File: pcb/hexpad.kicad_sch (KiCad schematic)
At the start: 12 parts, among them SW1 SW_Push, SW2 SW_Push, SW3 SW_Push, SW4 SW_Push, SW5 SW_Push, SW6 SW_Push, U1 XIAO-RP2040

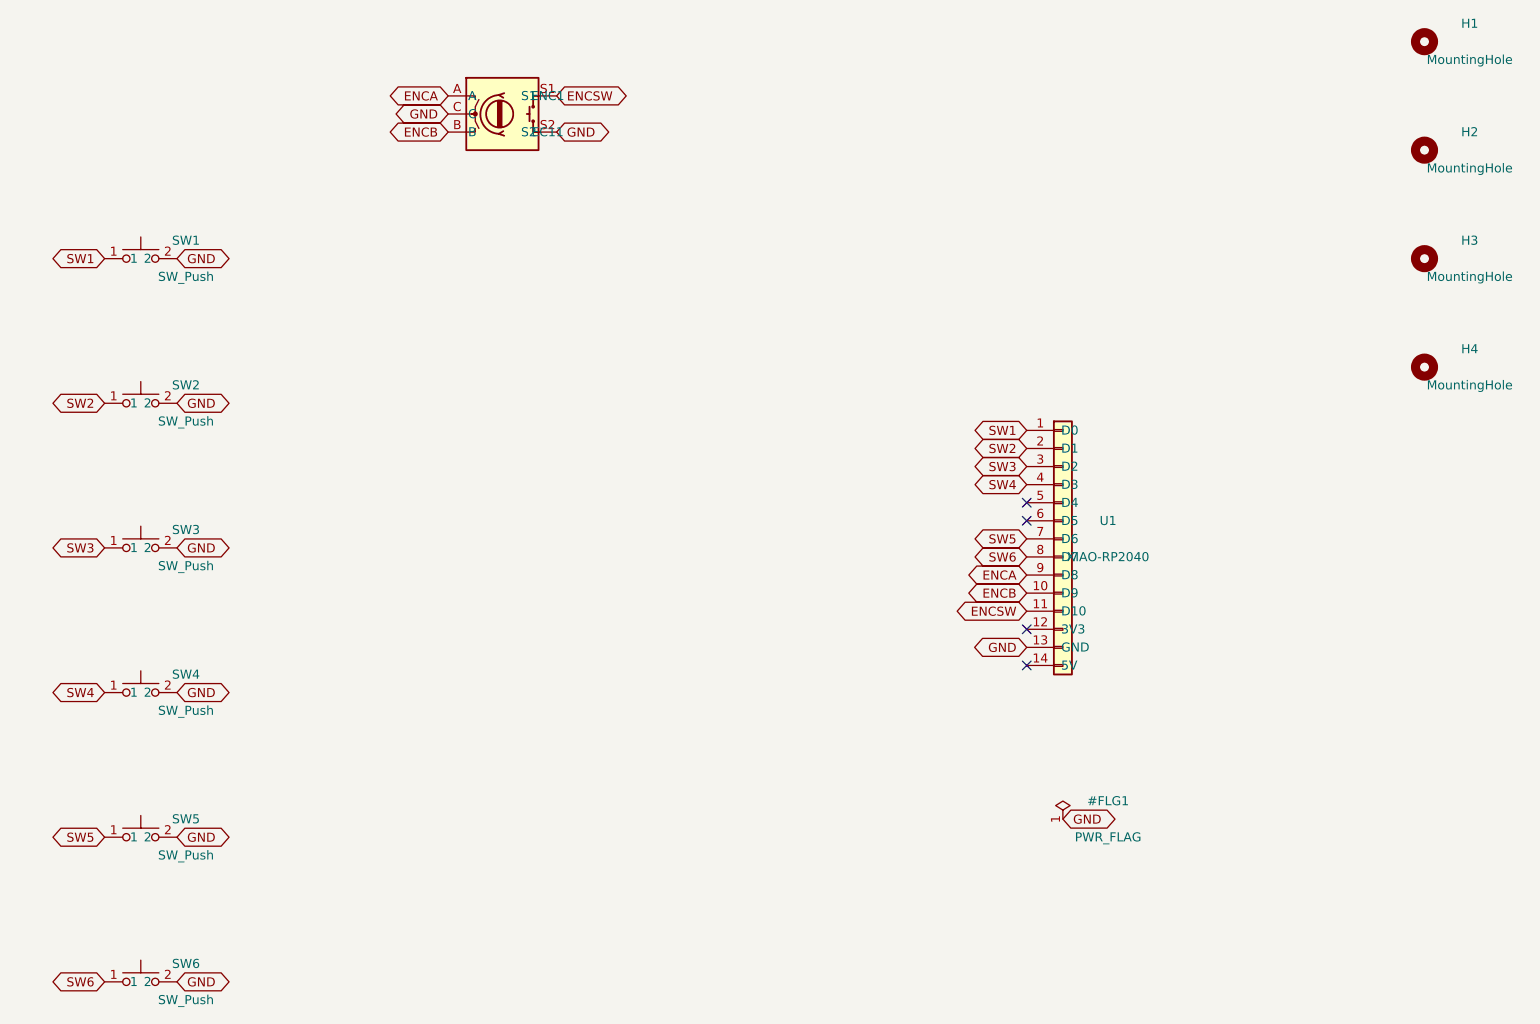
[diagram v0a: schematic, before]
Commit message: schematic: add wire stubs so labels don't overlap symbols
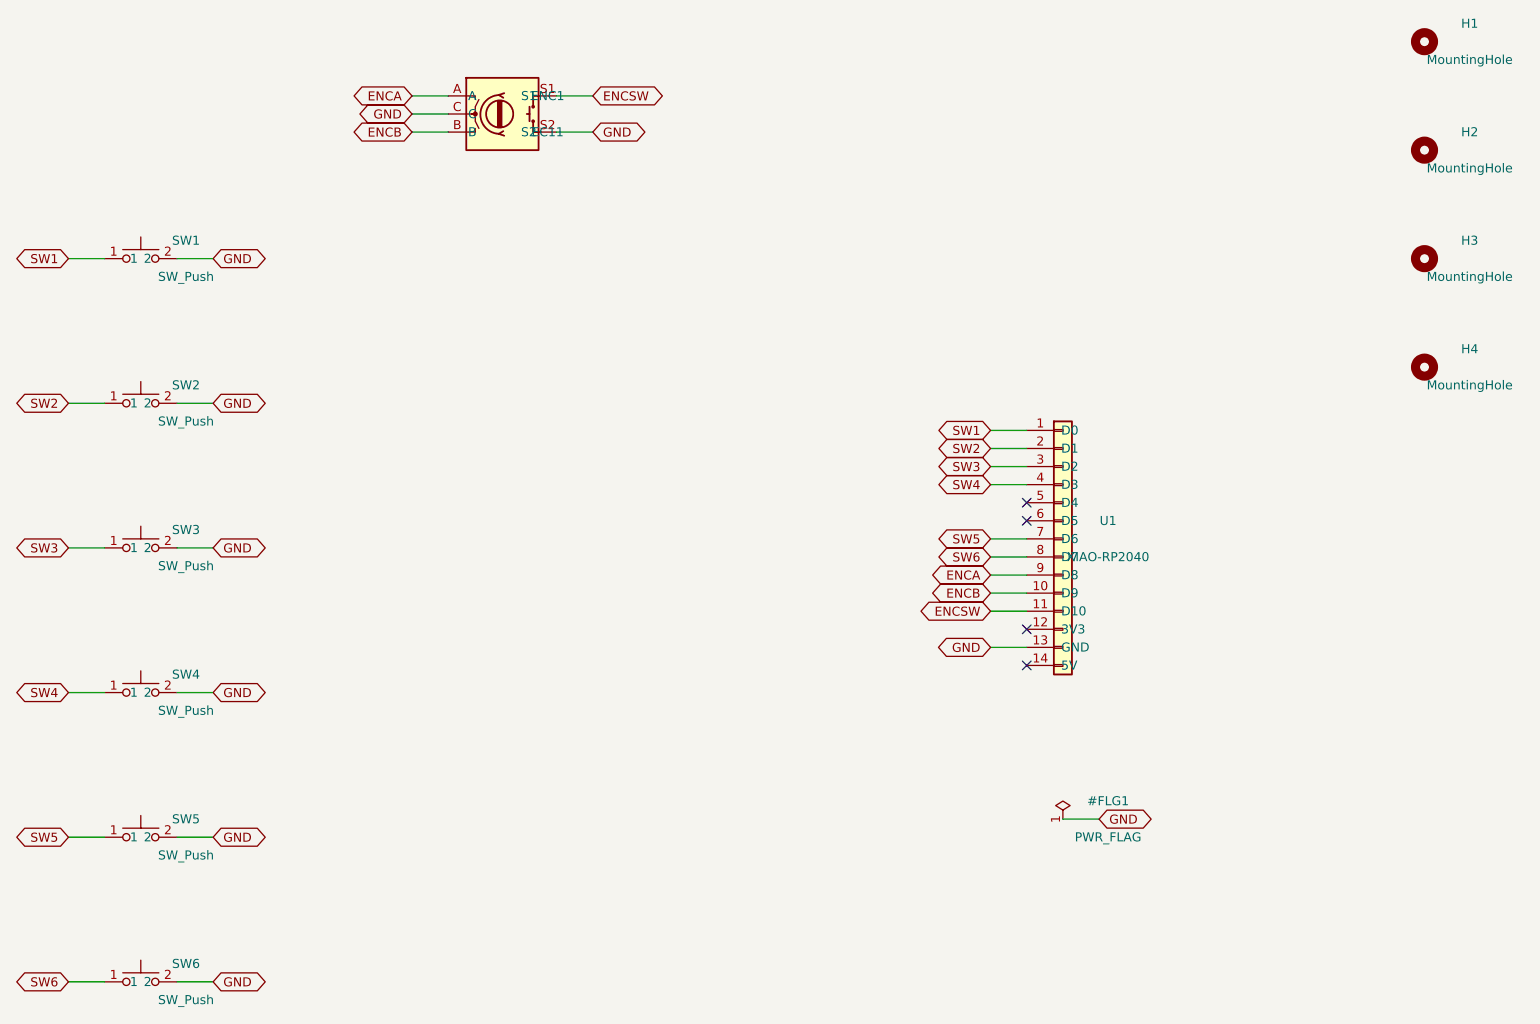
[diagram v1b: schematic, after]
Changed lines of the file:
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@@
   (no_connect (at 185.42 123.19))
   (no_connect (at 185.42 128.26999999999998))
-  (global_label "SW1" (shape bidirectional) (at 185.42 95.25 180)
+  (wire (pts (xy 185.42000000000002 95.25) (xy 180.34 95.25))
+    (stroke (width 0.0))
+  )
+  (wire (pts (xy 185.42000000000002 97.79) (xy 180.34 97.79))
+    (stroke (width 0.0))
+  )
+  (wire (pts (xy 185.42000000000002 100.33) (xy 180.34 100.33))
+    (stroke (width 0.0))
+  )
+  (wire (pts (xy 185.42000000000002 102.87) (xy 180.34 102.87))
+    (stroke (width 0.0))
+  )
+  (wire (pts (xy 185.42000000000002 110.49) (xy 180.34 110.49))
+    (stroke (width 0.0))
+  )
+  (wire (pts (xy 185.42000000000002 113.03) (xy 180.34 113.03))
+    (stroke (width 0.0))
+  )
+  (wire (pts (xy 185.42000000000002 115.57000000000001) (xy 180.34 115.57000000000001))
+    (stroke (width 0.0))
+  )
+  (wire (pts (xy 185.42000000000002 118.11) (xy 180.34 118.11))
+    (stroke (width 0.0))
+  )
+  (wire (pts (xy 185.42000000000002 120.65) (xy 180.34 120.65))
+    (stroke (width 0.0))
+  )
+  (wire (pts (xy 185.42000000000002 125.73) (xy 180.34 125.73))
+    (stroke (width 0.0))
+  )
+  (wire (pts (xy 55.88 71.12) (xy 50.8 71.12))
+    (stroke (width 0.0))
+  )
+  (wire (pts (xy 66.04 71.12) (xy 71.12 71.12))
+    (stroke (width 0.0))
+  )
+  (wire (pts (xy 55.88 91.44) (xy 50.8 91.44))
+    (stroke (width 0.0))
+  )
+  (wire (pts (xy 66.04 91.44) (xy 71.12 91.44))
+    (stroke (width 0.0))
+  )
+  (wire (pts (xy 55.88 111.76) (xy 50.8 111.76))
+    (stroke (width 0.0))
+  )
+  (wire (pts (xy 66.04 111.76) (xy 71.12 111.76))
+    (stroke (width 0.0))
+  )
+  (wire (pts (xy 55.88 132.08) (xy 50.8 132.08))
+    (stroke (width 0.0))
+  )
+  (wire (pts (xy 66.04 132.08) (xy 71.12 132.08))
+    (stroke (width 0.0))
+  )
+  (wire (pts (xy 55.88 152.4) (xy 50.8 152.4))
+    (stroke (width 0.0))
+  )
+  (wire (pts (xy 66.04 152.4) (xy 71.12 152.4))
+    (stroke (width 0.0))
+  )
+  (wire (pts (xy 55.88 172.72) (xy 50.8 172.72))
+    (stroke (width 0.0))
+  )
+  (wire (pts (xy 66.04 172.72) (xy 71.12 172.72))
+    (stroke (width 0.0))
+  )
+  (wire (pts (xy 104.14 48.26) (xy 99.06 48.26))
+    (stroke (width 0.0))
+  )
+  (wire (pts (xy 104.14 53.34) (xy 99.06 53.34))
+    (stroke (width 0.0))
+  )
+  (wire (pts (xy 104.14 50.8) (xy 99.06 50.8))
+    (stroke (width 0.0))
+  )
+  (wire (pts (xy 119.38 48.26) (xy 124.46000000000001 48.26))
+    (stroke (width 0.0))
+  )
+  (wire (pts (xy 119.38 53.34) (xy 124.46000000000001 53.34))
+    (stroke (width 0.0))
+  )
+  (wire (pts (xy 190.5 149.86) (xy 195.58 149.86))
+    (stroke (width 0.0))
+  )
+  (global_label "SW1" (shape bidirectional) (at 180.33999999999997 95.25 180)
     (effects (font (size 1.27 1.27)))
   )
-  (global_label "SW2" (shape bidirectional) (at 185.42 97.78999999999999 180)
+  (global_label "SW2" (shape bidirectional) (at 180.33999999999997 97.78999999999999 180)
     (effects (font (size 1.27 1.27)))
   )
-  (global_label "SW3" (shape bidirectional) (at 185.42 100.33 180)
+  (global_label "SW3" (shape bidirectional) (at 180.33999999999997 100.33 180)
     (effects (font (size 1.27 1.27)))
   )
-  (global_label "SW4" (shape bidirectional) (at 185.42 102.86999999999999 180)
+  (global_label "SW4" (shape bidirectional) (at 180.33999999999997 102.86999999999999 180)
     (effects (font (size 1.27 1.27)))
   )
-  (global_label "SW5" (shape bidirectional) (at 185.42 110.49 180)
+  (global_label "SW5" (shape bidirectional) (at 180.33999999999997 110.49 180)
     (effects (font (size 1.27 1.27)))
   )
-  (global_label "SW6" (shape bidirectional) (at 185.42 113.03 180)
+  (global_label "SW6" (shape bidirectional) (at 180.33999999999997 113.03 180)
     (effects (font (size 1.27 1.27)))
   )
-  (global_label "ENCA" (shape bidirectional) (at 185.42 115.57 180)
+  (global_label "ENCA" (shape bidirectional) (at 180.33999999999997 115.57 180)
     (effects (font (size 1.27 1.27)))
   )
-  (global_label "ENCB" (shape bidirectional) (at 185.42 118.11 180)
+  (global_label "ENCB" (shape bidirectional) (at 180.33999999999997 118.11 180)
     (effects (font (size 1.27 1.27)))
   )
-  (global_label "ENCSW" (shape bidirectional) (at 185.42 120.64999999999999 180)
+  (global_label "ENCSW" (shape bidirectional) (at 180.33999999999997 120.64999999999999 180)
     (effects (font (size 1.27 1.27)))
   )
-  (global_label "GND" (shape bidirectional) (at 185.42 125.72999999999999 180)
+  (global_label "GND" (shape bidirectional) (at 180.33999999999997 125.72999999999999 180)
     (effects (font (size 1.27 1.27)))
   )
-  (global_label "SW1" (shape bidirectional) (at 55.88 71.12 180)
+  (global_label "SW1" (shape bidirectional) (at 50.800000000000004 71.12 180)
     (effects (font (size 1.27 1.27)))
   )
-  (global_label "GND" (shape bidirectional) (at 66.04 71.12 0)
+  (global_label "GND" (shape bidirectional) (at 71.12 71.12 0)
     (effects (font (size 1.27 1.27)))
   )
-  (global_label "SW2" (shape bidirectional) (at 55.88 91.44 180)
+  (global_label "SW2" (shape bidirectional) (at 50.800000000000004 91.44 180)
     (effects (font (size 1.27 1.27)))
   )
-  (global_label "GND" (shape bidirectional) (at 66.04 91.44 0)
+  (global_label "GND" (shape bidirectional) (at 71.12 91.44 0)
     (effects (font (size 1.27 1.27)))
   )
-  (global_label "SW3" (shape bidirectional) (at 55.88 111.76 180)
+  (global_label "SW3" (shape bidirectional) (at 50.800000000000004 111.76 180)
     (effects (font (size 1.27 1.27)))
   )
-  (global_label "GND" (shape bidirectional) (at 66.04 111.76 0)
+  (global_label "GND" (shape bidirectional) (at 71.12 111.76 0)
     (effects (font (size 1.27 1.27)))
   )
-  (global_label "SW4" (shape bidirectional) (at 55.88 132.08 180)
+  (global_label "SW4" (shape bidirectional) (at 50.800000000000004 132.08 180)
     (effects (font (size 1.27 1.27)))
   )
-  (global_label "GND" (shape bidirectional) (at 66.04 132.08 0)
+  (global_label "GND" (shape bidirectional) (at 71.12 132.08 0)
     (effects (font (size 1.27 1.27)))
   )
-  (global_label "SW5" (shape bidirectional) (at 55.88 152.4 180)
+  (global_label "SW5" (shape bidirectional) (at 50.800000000000004 152.4 180)
     (effects (font (size 1.27 1.27)))
   )
-  (global_label "GND" (shape bidirectional) (at 66.04 152.4 0)
+  (global_label "GND" (shape bidirectional) (at 71.12 152.4 0)
     (effects (font (size 1.27 1.27)))
   )
-  (global_label "SW6" (shape bidirectional) (at 55.88 172.72 180)
+  (global_label "SW6" (shape bidirectional) (at 50.800000000000004 172.72 180)
     (effects (font (size 1.27 1.27)))
   )
-  (global_label "GND" (shape bidirectional) (at 66.04 172.72 0)
+  (global_label "GND" (shape bidirectional) (at 71.12 172.72 0)
     (effects (font (size 1.27 1.27)))
   )
-  (global_label "ENCA" (shape bidirectional) (at 104.14 48.26 180)
+  (global_label "ENCA" (shape bidirectional) (at 99.06 48.26 180)
     (effects (font (size 1.27 1.27)))
   )
-  (global_label "ENCB" (shape bidirectional) (at 104.14 53.339999999999996 180)
+  (global_label "ENCB" (shape bidirectional) (at 99.06 53.339999999999996 180)
     (effects (font (size 1.27 1.27)))
   )
-  (global_label "GND" (shape bidirectional) (at 104.14 50.8 180)
+  (global_label "GND" (shape bidirectional) (at 99.06 50.8 180)
     (effects (font (size 1.27 1.27)))
   )
-  (global_label "ENCSW" (shape bidirectional) (at 119.38000000000001 48.26 0)
+  (global_label "ENCSW" (shape bidirectional) (at 124.46000000000001 48.26 0)
     (effects (font (size 1.27 1.27)))
   )
-  (global_label "GND" (shape bidirectional) (at 119.38000000000001 53.339999999999996 0)
+  (global_label "GND" (shape bidirectional) (at 124.46000000000001 53.339999999999996 0)
     (effects (font (size 1.27 1.27)))
   )
-  (global_label "GND" (shape bidirectional) (at 190.5 149.86 0)
+  (global_label "GND" (shape bidirectional) (at 195.58 149.86 0)
     (effects (font (size 1.27 1.27)))
   )
